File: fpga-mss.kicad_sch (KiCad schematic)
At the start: 7 parts, among them U1 MPFS250T-FCVG484, Y3 Oscillator_125MHz_DSC1103DI2

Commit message: [#57422] Finishing touches
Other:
- moved on the sheet: C4, R60, R74, R75, R87, U1F, U1G, Y3

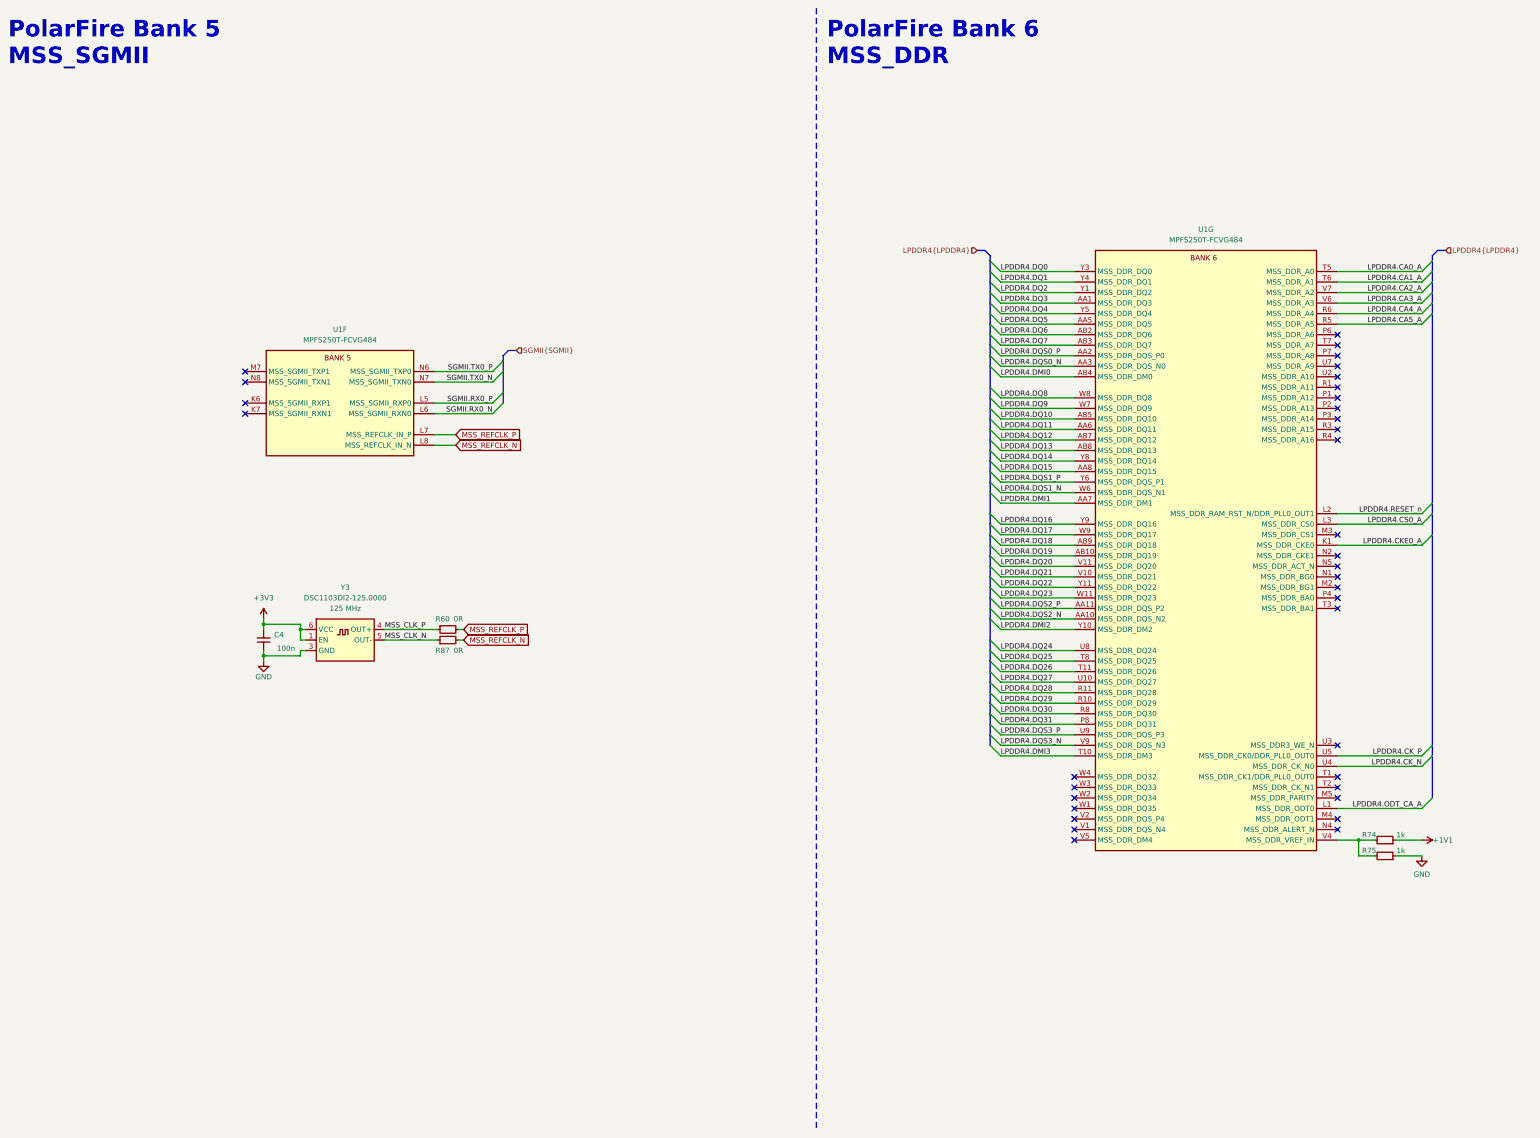
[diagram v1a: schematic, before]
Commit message: [#57422] Align schematics
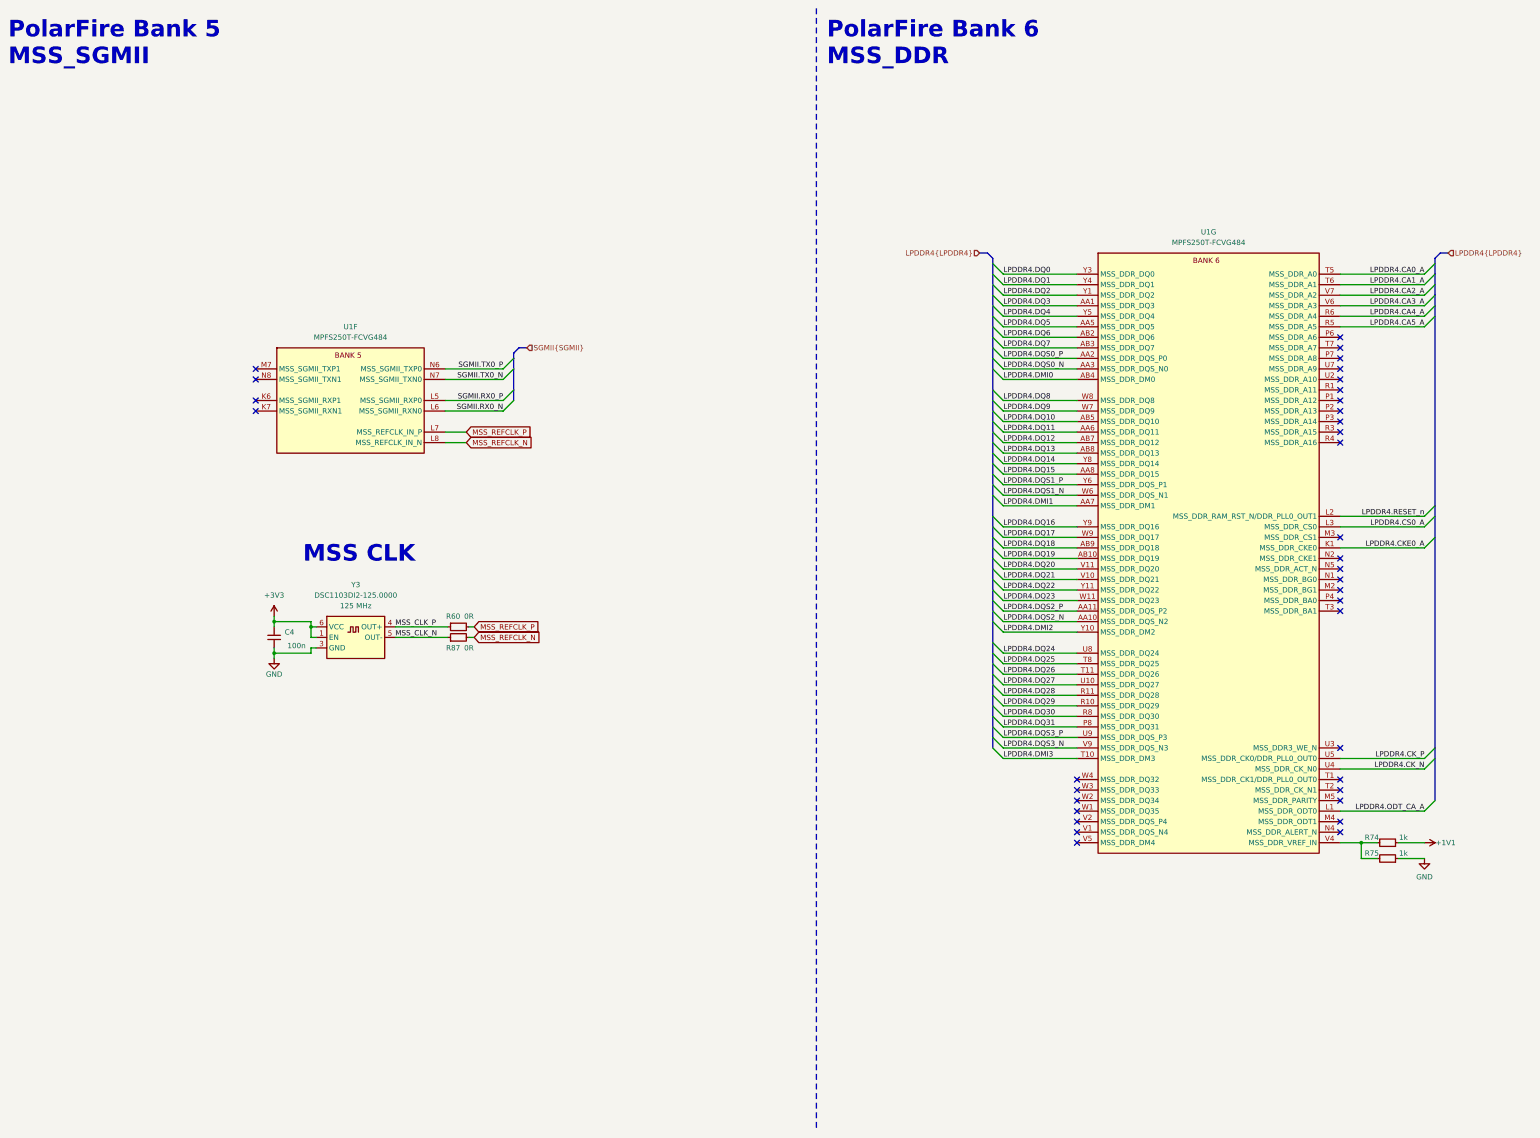
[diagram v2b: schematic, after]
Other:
- note added: "MSS CLK"
- moved on the sheet: C4, R60, R74, R75, R87, U1F, U1G, Y3
